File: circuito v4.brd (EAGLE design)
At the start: 91.5 x 57.8 mm, 64 parts, among them IC1 LM324N

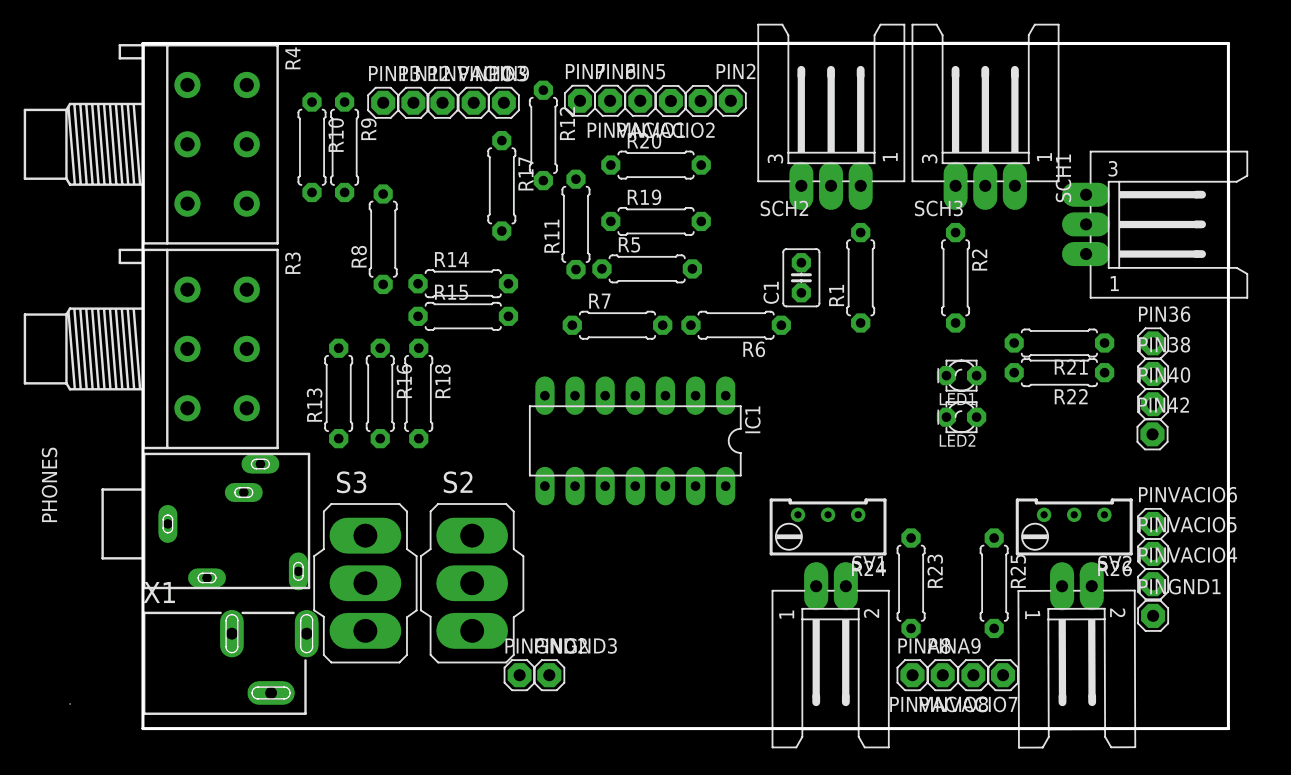
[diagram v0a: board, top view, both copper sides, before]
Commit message: Layout tal que el routeado da 17 vias
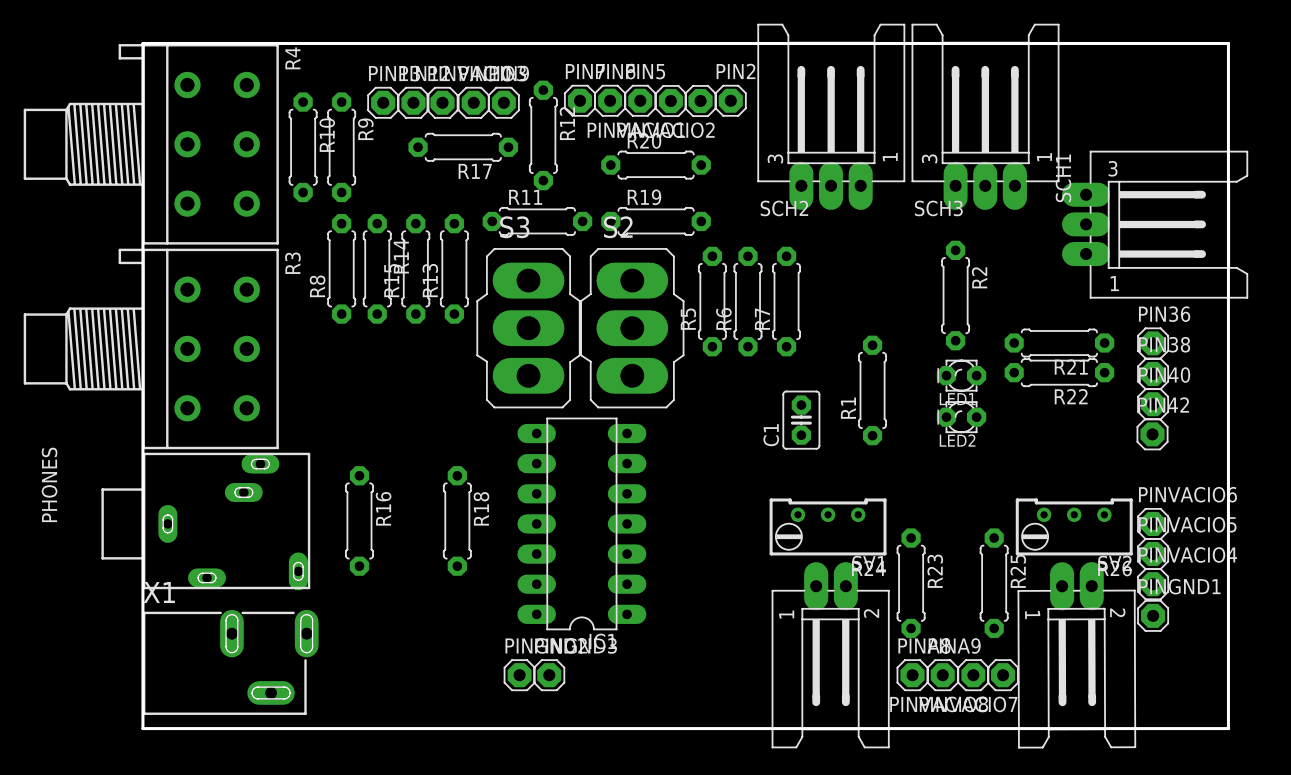
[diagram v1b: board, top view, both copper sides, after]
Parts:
- moved S3 25.5 mm to (41.2, 31.8)
- moved S2 25.4 mm to (50.0, 31.8)
- moved R7 14.4 mm to (63.0, 34.0), turned to 90 degrees
- moved R13 14.3 mm to (35.0, 36.8)
- moved C1 12.0 mm to (64.2, 24.0)
- moved R18 11.2 mm to (35.2, 15.5)
- moved R16 10.9 mm to (27.0, 15.5)
- moved R1 9.55 mm to (70.2, 26.5)
- moved IC1 8.32 mm to (45.8, 15.2), turned to 90 degrees
- moved R14 7.36 mm to (28.5, 36.8), turned to 270 degrees
- moved R5 6.15 mm to (56.8, 34.0), turned to 90 degrees
- moved R15 5.66 mm to (31.8, 36.8), turned to 90 degrees
- moved R17 4.60 mm to (35.8, 47.0), turned to 180 degrees
- moved R8 4.30 mm to (25.5, 36.8)
- moved R11 3.26 mm to (42.0, 40.8), turned to 0 degrees
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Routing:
- removed copper zone on layer 16, net N$10

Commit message: Layout tal que el routeado da 9 vias
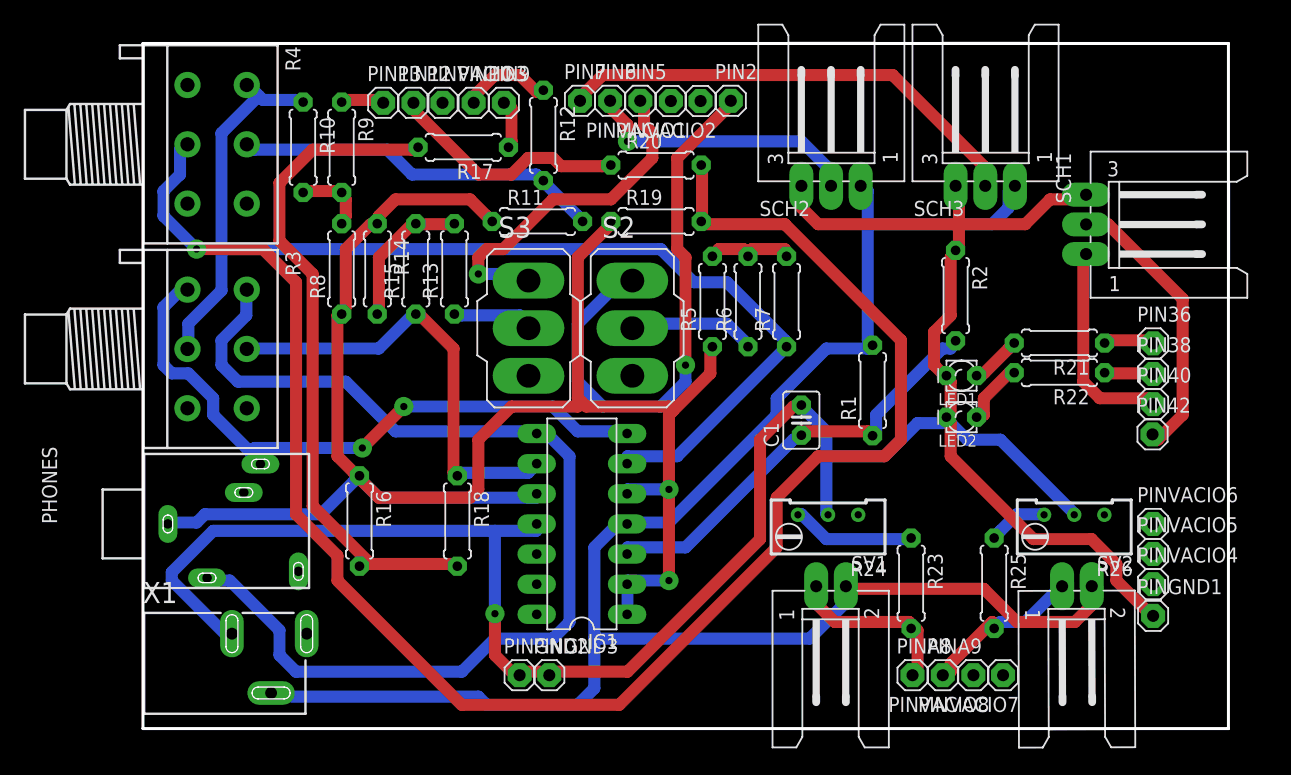
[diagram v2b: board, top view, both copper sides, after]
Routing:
- net GND: track 0.00 -> 204.2 mm, vias 0 -> 1
- net N$8: track 0.00 -> 150.7 mm, vias 0 -> 2
- net VCC: track 0.00 -> 148.1 mm
- net N$18: track 0.00 -> 144.8 mm, vias 0 -> 1
- net N$4: track 0.00 -> 98.2 mm
- net N$30: track 0.00 -> 90.7 mm
- net N$19: track 0.00 -> 56.6 mm
- net N$37: track 0.00 -> 54.2 mm, vias 0 -> 2
- net N$7: track 0.00 -> 48.1 mm, vias 0 -> 1
- net N$28: track 0.00 -> 40.2 mm
- net N$13: track 0.00 -> 37.8 mm
- net N$1: track 0.00 -> 36.8 mm
- net N$11: track 0.00 -> 31.0 mm
- net N$16: track 0.00 -> 29.5 mm, vias 0 -> 1
- net N$22: track 0.00 -> 24.1 mm
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
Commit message: Layout 100% y 10 vias
Hay que restringirle la posibilidad de vias debajo de los componentes
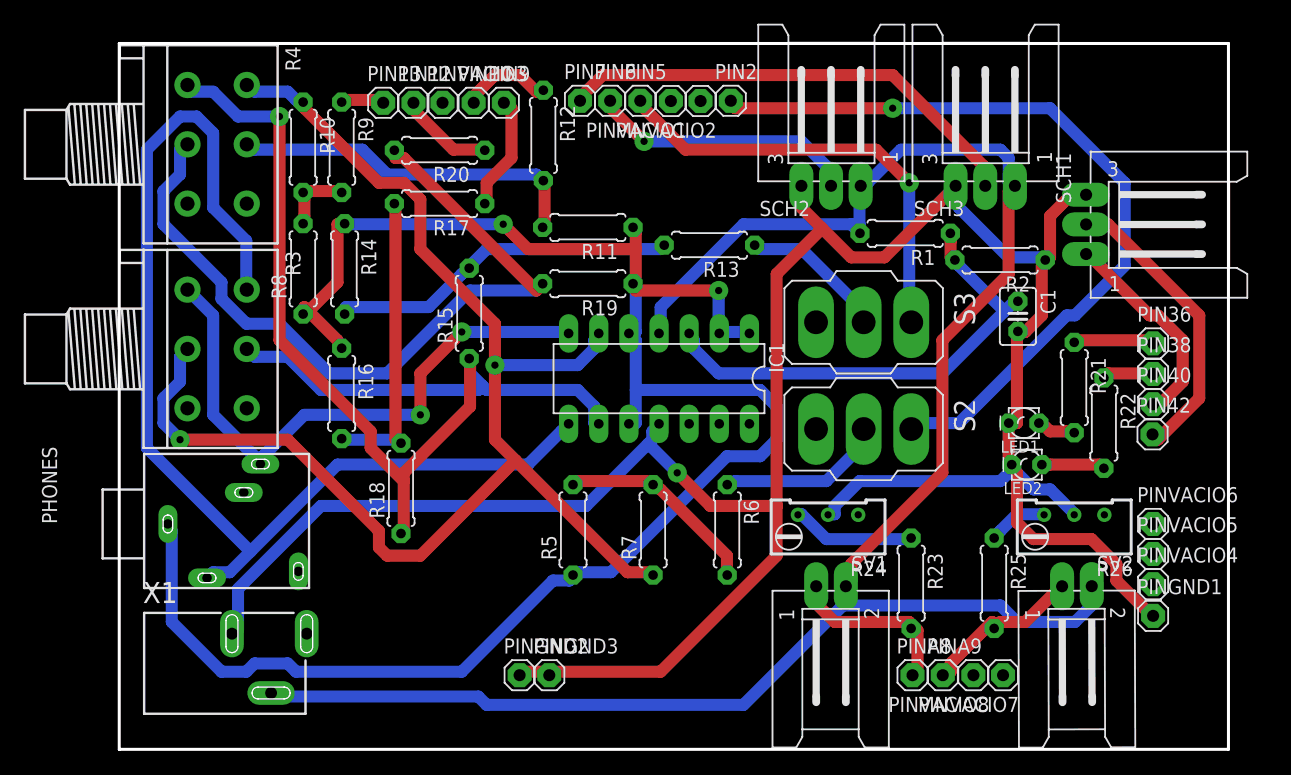
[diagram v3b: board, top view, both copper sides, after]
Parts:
- moved S3 28.3 mm to (69.5, 32.2), turned to 270 degrees
- moved R5 22.6 mm to (45.0, 14.8)
- moved R7 22.3 mm to (51.8, 14.8)
- moved R13 21.6 mm to (56.5, 38.8), turned to 180 degrees
- moved S2 21.3 mm to (69.5, 23.2), turned to 270 degrees
- moved C1 20.2 mm to (82.5, 32.8), turned to 270 degrees
- moved R6 19.3 mm to (58.0, 14.8), turned to 270 degrees
- moved R20 18.3 mm to (33.8, 46.8), turned to 180 degrees
- moved IC1 13.9 mm to (52.2, 27.5), turned to 180 degrees
- moved R1 13.5 mm to (73.0, 39.8), turned to 180 degrees
- moved R16 10.9 mm to (25.5, 26.2)
- moved R19 7.79 mm to (46.2, 35.5), turned to 180 degrees
- moved LED2 6.80 mm to (83.2, 20.2)
- moved LED1 6.60 mm to (83.0, 23.8)
- moved R15 5.86 mm to (36.2, 33.0)
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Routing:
- net N$18: track 144.8 -> 66.7 mm, vias 1 -> 0
- net N$13: track 37.8 -> 97.5 mm, vias 0 -> 1
- net N$19: track 56.6 -> 25.6 mm
- net N$7: track 48.1 -> 66.8 mm
- net N$4: track 98.2 -> 115.6 mm, vias 0 -> 2
- net N$14: track 12.3 -> 29.6 mm
- net VCC: track 148.1 -> 162.0 mm
- net GND: track 204.2 -> 217.2 mm
- net N$21: track 20.4 -> 8.05 mm
- net N$5: track 7.72 -> 17.4 mm
- net N$16: track 29.5 -> 37.4 mm
- net N$8: track 150.7 -> 156.6 mm
- net N$15: track 6.89 -> 12.6 mm
- net N$20: track 4.14 -> 9.73 mm
- net N$30: track 90.7 -> 95.0 mm
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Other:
- board size 91.5 x 57.8 mm -> 93.5 x 59.5 mm

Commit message: Agregado de restriccion de vias
Se agregan poligonos en la capa vRestrict debajo de conectores, potes, phones, X1 y resistencias variables
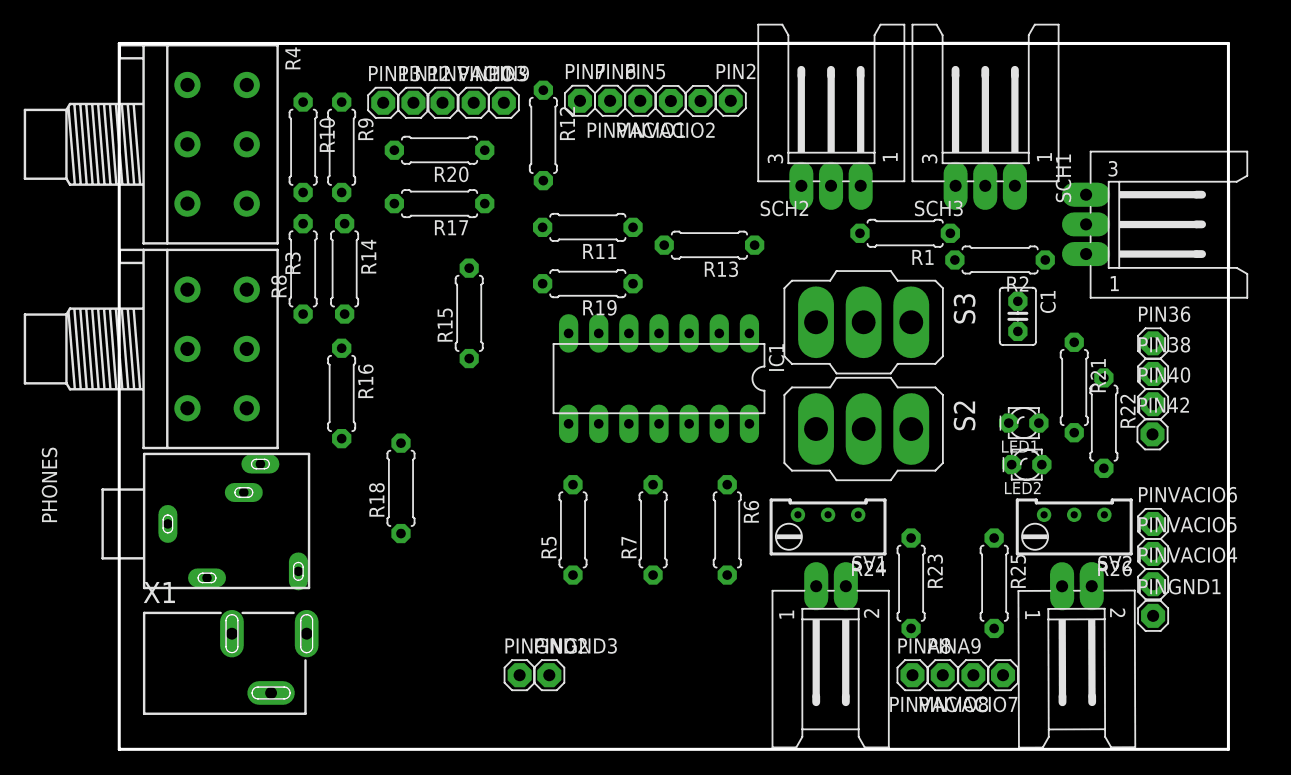
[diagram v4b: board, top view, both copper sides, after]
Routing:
- net GND: track 217.2 -> 0.00 mm, vias 1 -> 0
- net VCC: track 162.0 -> 0.00 mm
- net N$8: track 156.6 -> 0.00 mm, vias 2 -> 0
- net N$4: track 115.6 -> 0.00 mm, vias 2 -> 0
- net N$13: track 97.5 -> 0.00 mm, vias 1 -> 0
- net N$30: track 95.0 -> 0.00 mm
- net N$7: track 66.8 -> 0.00 mm, vias 1 -> 0
- net N$18: track 66.7 -> 0.00 mm
- net N$37: track 50.1 -> 0.00 mm, vias 2 -> 0
- net N$1: track 40.8 -> 0.00 mm
- net N$28: track 40.2 -> 0.00 mm
- net N$16: track 37.4 -> 0.00 mm, vias 1 -> 0
- net N$11: track 30.2 -> 0.00 mm
- net N$14: track 29.6 -> 0.00 mm
- net N$19: track 25.6 -> 0.00 mm
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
